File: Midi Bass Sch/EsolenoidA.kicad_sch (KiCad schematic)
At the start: 60 parts

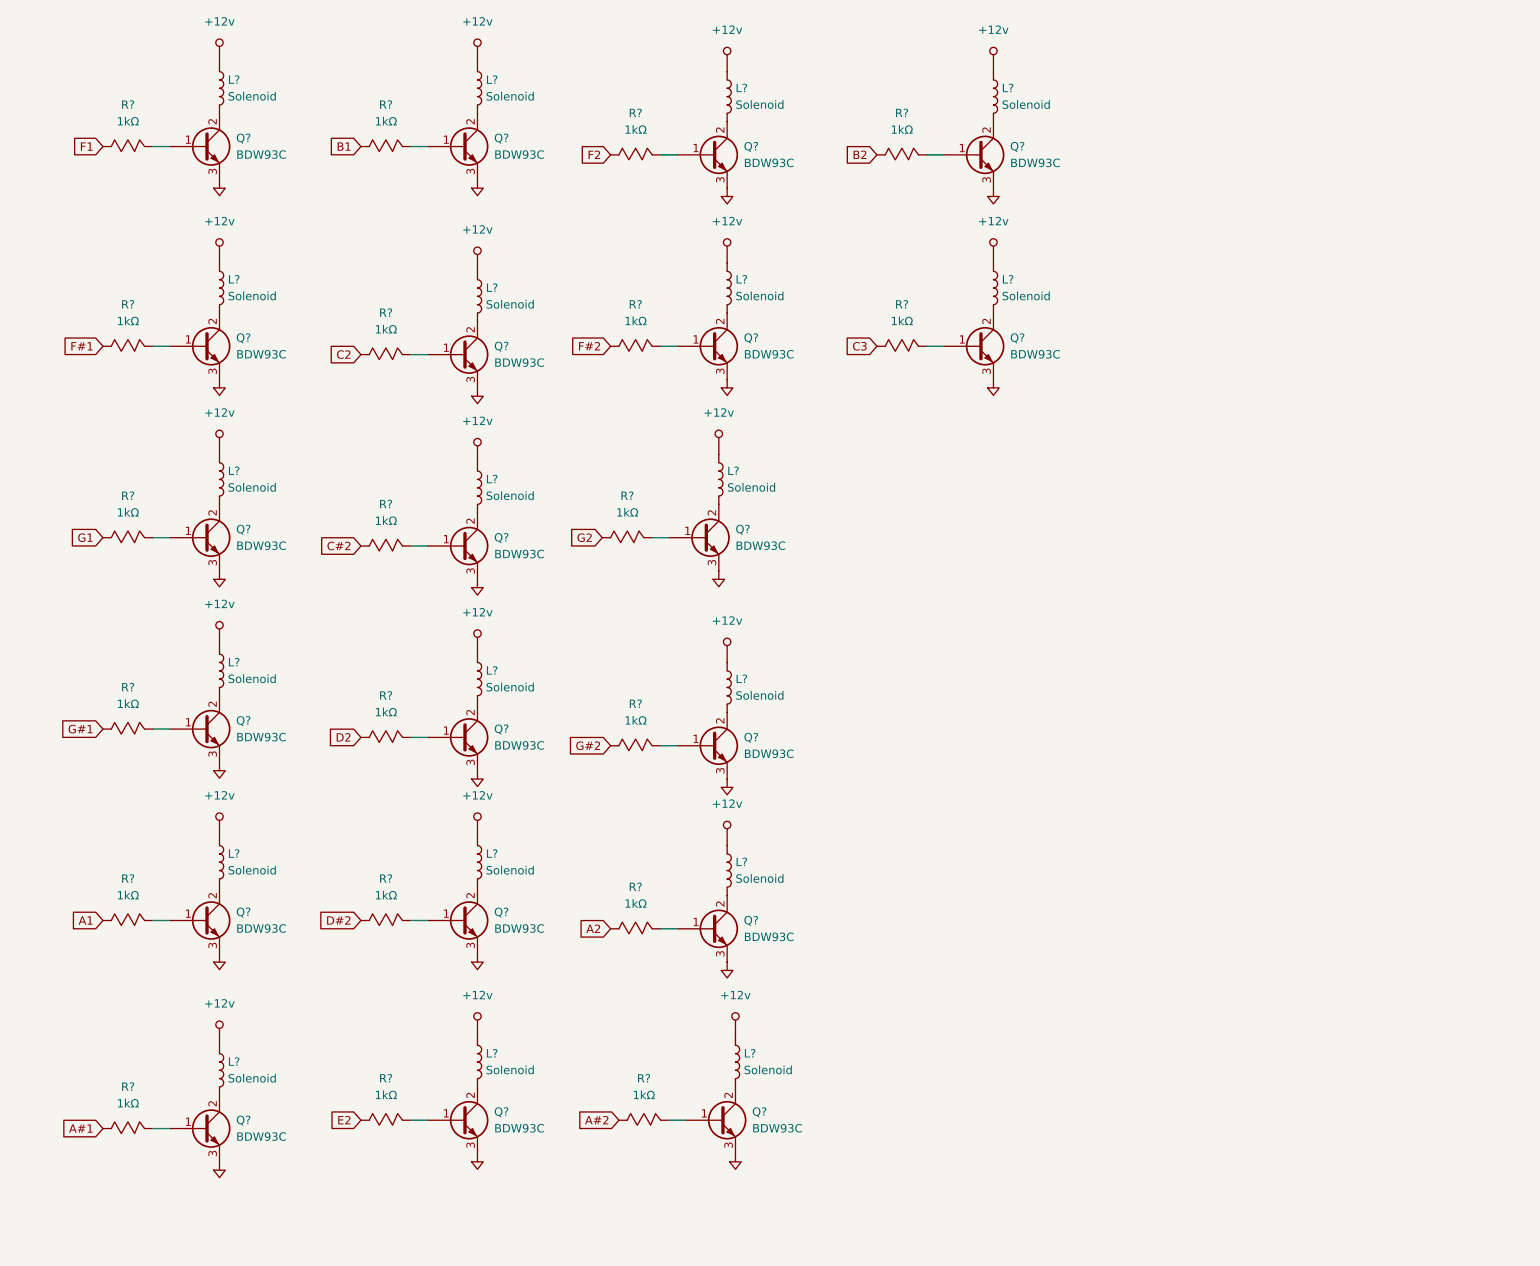
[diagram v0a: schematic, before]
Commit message: updated schematic numbers
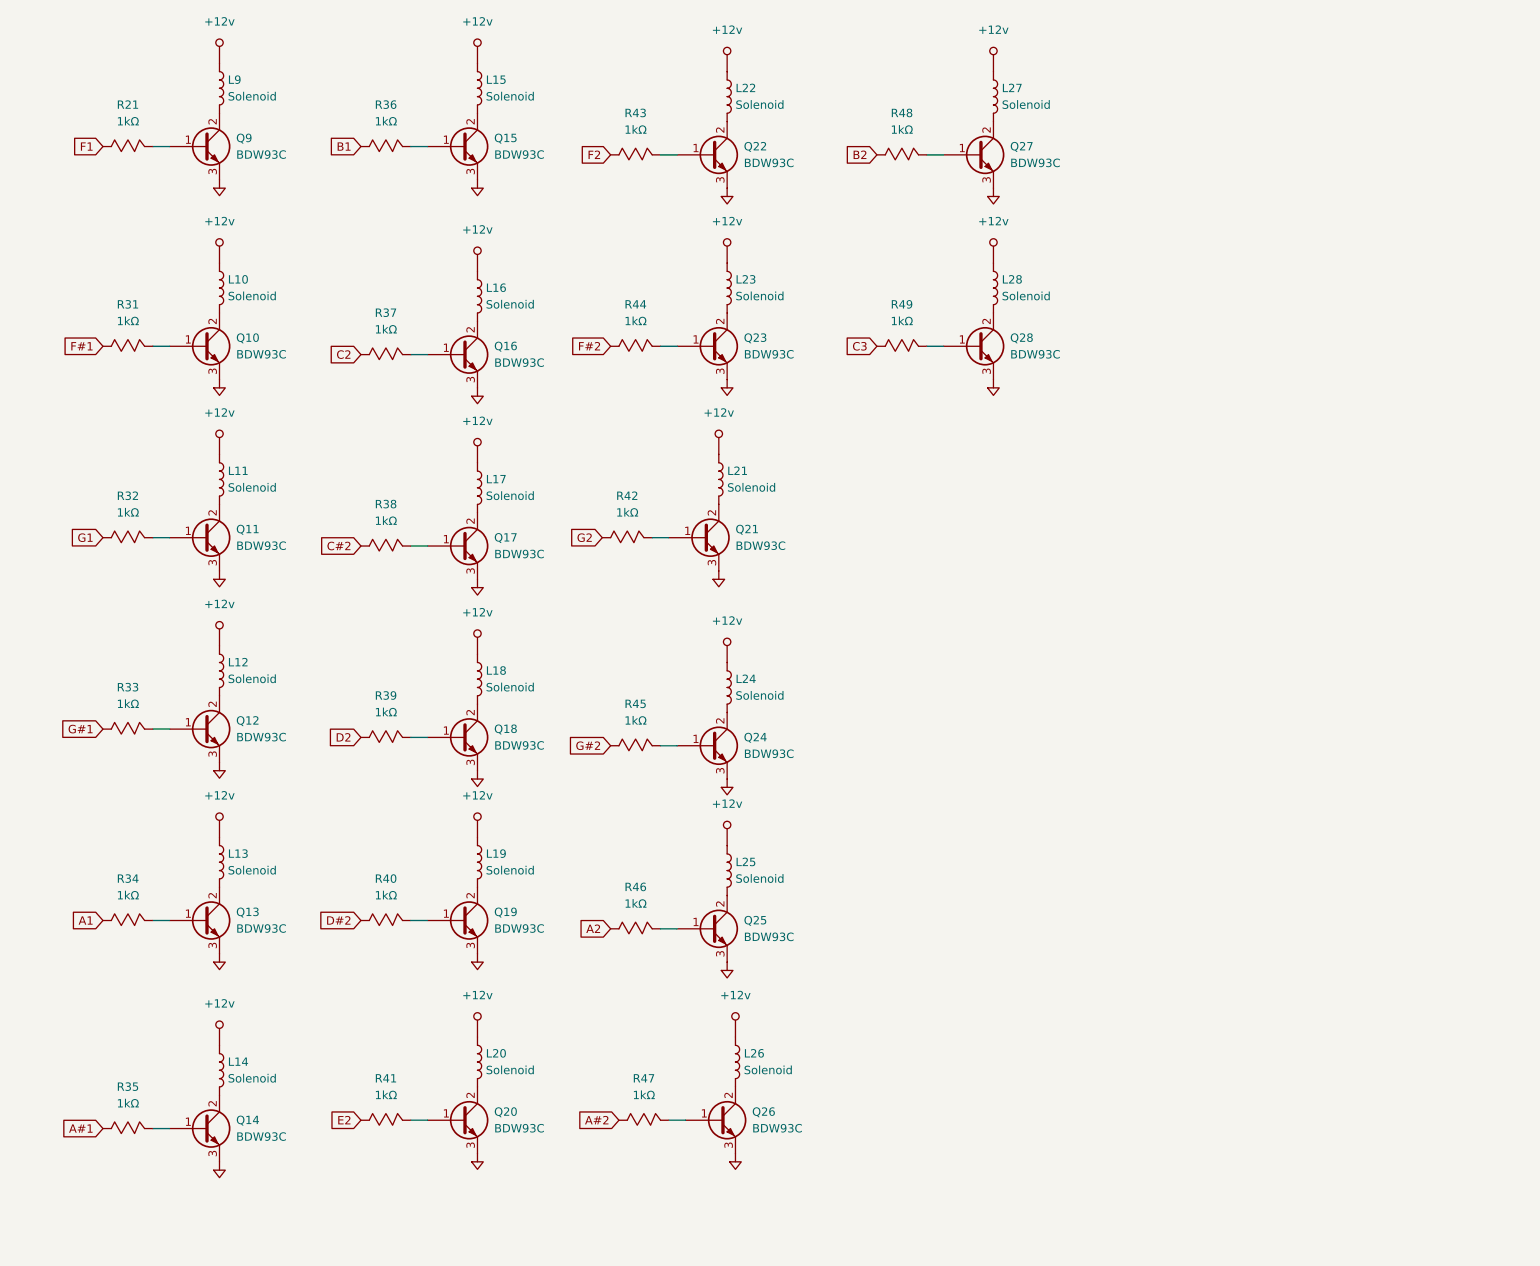
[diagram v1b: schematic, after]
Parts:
- gave numbers to parts that had none: 60

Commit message: updated solenoid array to use opto isolation
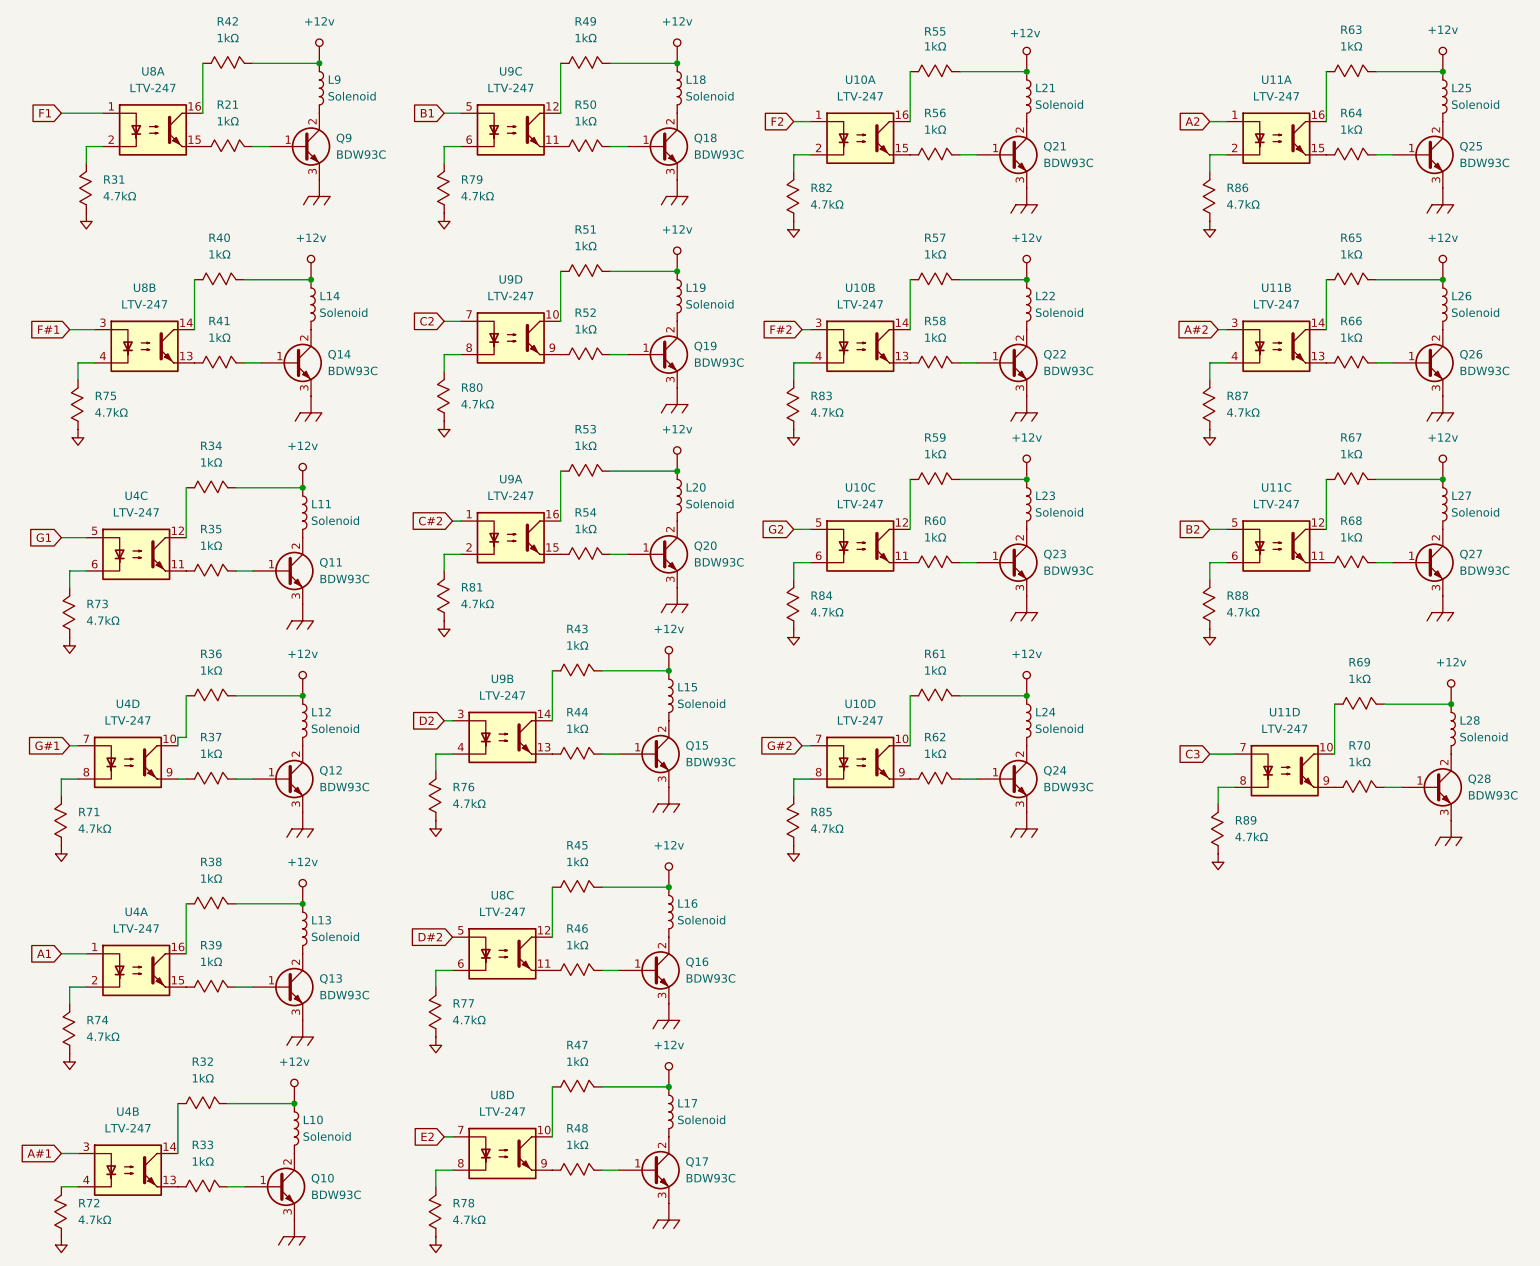
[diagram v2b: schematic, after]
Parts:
- removed R31: 1kΩ, symbol Custom Symbols:Resistor_Mod
- added R31, R71, R72, R73, R74, R75, R76, R77, R78, R79, R80, R81, R82, R83, R84, R85, R86, R87, R88, R89: 4.7kΩ, symbol Owen's Symbols:Resistor_Mod
- added R50, R51, R52, R53, R54, R55, R56, R57, R58, R59, R60, R61, R62, R63, R64, R65, R66, R67, R68, R69, R70: 1kΩ, symbol Custom Symbols:Resistor_Mod
- added U10, U11, U4, U8, U9: LTV-247, Package_SO:SOP-16_4.4x10.4mm_P1.27mm, symbol Isolator:LTV-247
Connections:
- net +12v: now also R32.2, R34.2, R36.2, R38.2, R40.2, R42.2, R43.2, R45.2, R47.2, R49.2, R51.2, R53.2, R55.2, R57.2, R59.2, R61.2, R63.2, R65.2, R67.2, R69.2
- net A#1: now also U4.3; no longer R35.1
- net A#2: now also U11.3; no longer R47.1
- net A1: now also U4.1; no longer R34.1
- net A2: now also U11.1; no longer R46.1
- net B1: now also U9.5; no longer R36.1
- net B2: now also U11.5; no longer R48.1
- net C#2: now also U9.1; no longer R38.1
- net C2: now also U9.7; no longer R37.1
- net C3: now also U11.7; no longer R49.1
- net D#2: now also U8.5; no longer R40.1
- net D2: now also U9.3; no longer R39.1
- net E2: now also U8.7; no longer R41.1
- net F#1: now also U8.3
- net F#2: now also U10.3; no longer R44.1
- net F1: now also U8.1; no longer R21.1
- net F2: now also U10.1; no longer R43.1
- net G#1: now also U4.7; no longer R33.1
- net G#2: now also U10.7; no longer R45.1
- net G1: now also U4.5; no longer R32.1
- net G2: now also U10.5; no longer R42.1
- net GND: now also R31.1, R71.1, R72.1, R73.1, R74.1, R75.1, R76.1, R77.1, R78.1, R79.1, R80.1, R81.1, R82.1, R83.1, R84.1, R85.1, R86.1, R87.1, R88.1, R89.1; no longer Q10.3 (E), Q11.3 (E), Q12.3 (E), Q13.3 (E), Q14.3 (E), Q15.3 (E), Q16.3 (E), Q17.3 (E), Q18.3 (E), Q19.3 (E), Q20.3 (E), Q21.3 (E), Q22.3 (E), Q23.3 (E), Q24.3 (E), Q25.3 (E), Q26.3 (E), Q27.3 (E), Q28.3 (E), Q9.3 (E)
- net at Q10.1 (B): now also R33.2
- net at Q11.1 (B): now also R35.2; no longer R32.2
- net at Q13.1 (B): now also R39.2; no longer R34.2
- net at Q16.1 (B): now also R46.2; no longer R37.2
- net at Q26.1 (B): now also R66.2; no longer R47.2
- net at Q21.1 (B): now also R56.2; no longer R42.2
- net at Q18.1 (B): now also R50.2; no longer R39.2
- net at Q22.1 (B): now also R58.2; no longer R43.2
- net at R44.2: now also Q15.1 (B); no longer Q23.1 (B)
- net at Q17.1 (B): now also R48.2; no longer R38.2
- net at Q25.1 (B): now also R64.2; no longer R46.2
- net at Q12.1 (B): now also R37.2; no longer R33.2
- net at Q19.1 (B): now also R52.2; no longer R40.2
- net at Q14.1 (B): now also R41.2; no longer R35.2
- net at Q24.1 (B): now also R62.2; no longer R45.2
- net at Q28.1 (B): now also R70.2; no longer R49.2
- net at Q27.1 (B): now also R68.2; no longer R48.2
- net at Q20.1 (B): now also R54.2; no longer R41.2
- new net: R58.1, U10.13
- new net: R61.1, U10.10
- new net: R85.2, U10.8
- new net: R62.1, U10.9
- new net: R33.1, U4.13
- new net: R32.1, U4.14
- new net: R72.2, U4.4
- new net: R35.1, U4.11
- new net: R86.2, U11.2
- new net: R53.1, U9.16
- new net: R60.1, U10.11
- new net: R59.1, U10.12
- new net: R84.2, U10.6
- new net: R39.1, U4.15
- new net: R38.1, U4.16
- new net: R74.2, U4.2
- new net: R51.1, U9.10
- new net: R66.1, U11.13
- new net: R65.1, U11.14
- new net: R87.2, U11.4
- new net: R44.1, U9.13
- new net: R88.2, U11.6
- new net: R21.1, U8.15
- new net: R42.1, U8.16
- new net: R31.2, U8.2
- new net: R64.1, U11.15
- new net: R46.1, U8.11
- new net: R45.1, U8.12
- new net: R77.2, U8.6
- new net: R36.1, U4.10
- new net: R71.2, U4.8
- new net: R37.1, U4.9
- new net: R56.1, U10.15
- new net: R55.1, U10.16
- new net: R82.2, U10.2
- new net: R47.1, U8.10
- new net: R50.1, U9.11
- new net: R80.2, U9.8
- new net: R52.1, U9.9
- new net: R40.1, U8.14
- new net: Q23.1 (B), R60.2
- new net: R63.1, U11.16
- new net: R49.1, U9.12
- new net: R78.2, U8.8
- new net: R57.1, U10.14
- new net: R81.2, U9.2
- new net: R48.1, U8.9
- new net: R79.2, U9.6
- new net: R43.1, U9.14
- new net: R70.1, U11.9
- new net: R54.1, U9.15
- new net: R34.1, U4.12
- new net: R73.2, U4.6
- new net: R89.2, U11.8
- new net: R83.2, U10.4
- new net: R67.1, U11.12
- new net: R76.2, U9.4
- new net: R41.1, U8.13
- new net: R75.2, U8.4
- new net: R68.1, U11.11
- new net: R69.1, U11.10
- new net Chassis_GND: Q10.3 (E), Q11.3 (E), Q12.3 (E), Q13.3 (E), Q14.3 (E), Q15.3 (E), Q16.3 (E), Q17.3 (E), Q18.3 (E), Q19.3 (E), Q20.3 (E), Q21.3 (E), Q22.3 (E), Q23.3 (E), Q24.3 (E), Q25.3 (E), Q26.3 (E), Q27.3 (E), Q28.3 (E), Q9.3 (E)
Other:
- moved on the sheet: L9, Q9, R21
